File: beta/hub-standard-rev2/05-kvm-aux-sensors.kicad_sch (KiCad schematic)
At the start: 16 parts

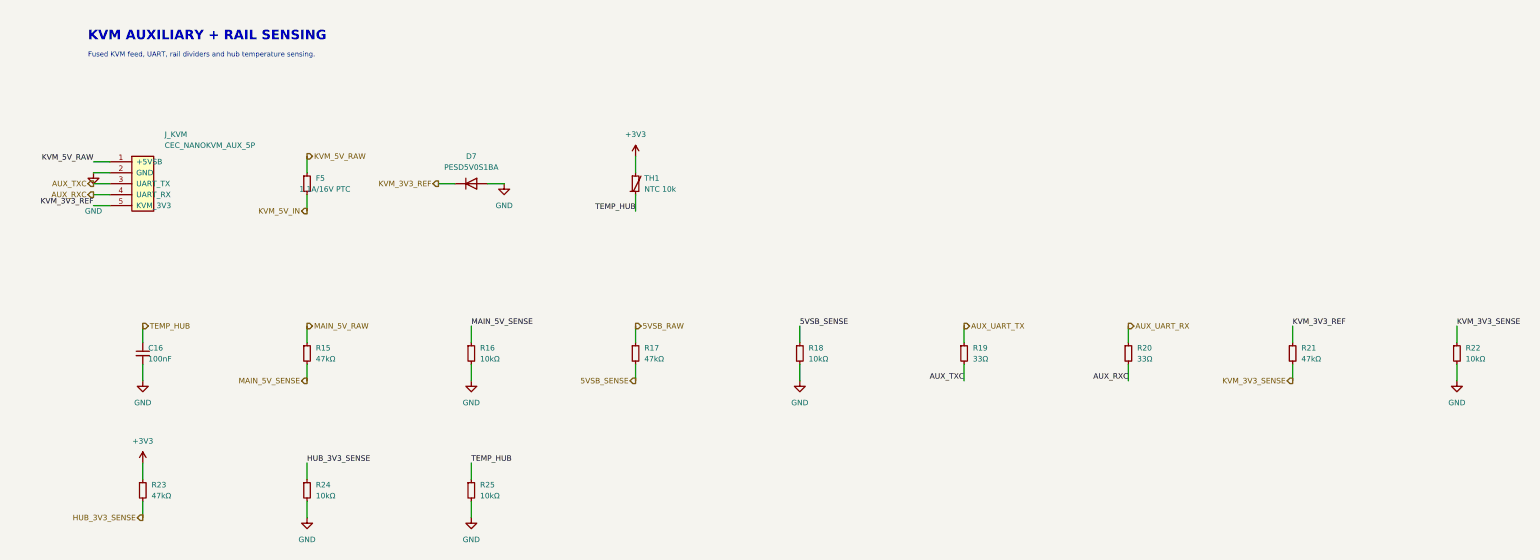
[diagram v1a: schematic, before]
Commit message: Rework BETA power rails and schematic composition
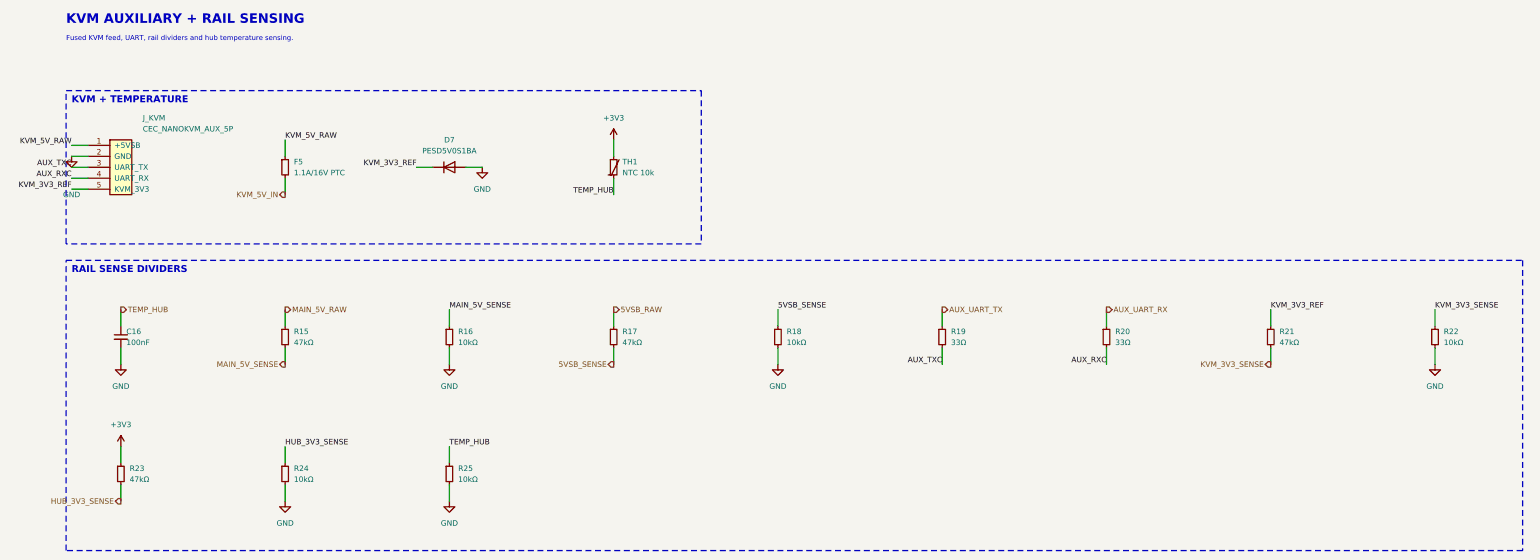
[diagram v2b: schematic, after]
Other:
- note added: "KVM + TEMPERATURE"
- note added: "RAIL SENSE DIVIDERS"

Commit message: pipeline: integrate route-aware physical design flow
Generalize critical-first placement and routing, future-congestion and power-authority planning, route provenance, process watchdogs, fab/thermal validation, dashboard review, and XFCN integration. Add the supporting board contracts, component libraries, documentation, and regression coverage.
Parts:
- removed R17: 47kΩ, cec-Resistor_SMD:R_0402_1005Metric, symbol cec-vendor:R_Small
- removed R18: 10kΩ, cec-Resistor_SMD:R_0402_1005Metric, symbol cec-vendor:R_Small
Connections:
- net MAIN_5V_RAW renamed +5V_SYS
- net MAIN_5V_SENSE renamed 5V_SYS_SENSE
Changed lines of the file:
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@@
-	)
-	(symbol
-		(lib_id "cec-vendor:R_Small")
-		(at 170.18 157.48 0)
-		(unit 1)
-		(exclude_from_sim no)
-		(in_bom yes)
-		(on_board yes)
-		(dnp no)
-		(fields_autoplaced yes)
-		(property "Reference" "R17" (at 172.212 156.21 0) (effects (font (size 1.27 1.27)) (justify left)))
-		(property "Value" "47kΩ" (at 172.212 158.75 0) (effects (font (size 1.27 1.27)) (justify left)))
-		(property "Footprint" "cec-Resistor_SMD:R_0402_1005Metric" (at 170.18 157.48 0) (effects (font (size 1.27 1.27)) (hide yes)))
-		(property "Datasheet" "" (at 170.18 157.48 0) (effects (font (size 1.27 1.27)) (hide yes)))
-		(property "Manufacturer" "UNI-ROYAL" (at 170.18 157.48 0) (effects (font (size 1.27 1.27)) (hide yes)))
-		(property "MPN" "0402WGF4702TCE" (at 170.18 157.48 0) (effects (font (size 1.27 1.27)) (hide yes)))
-		(property "LCSC" "C25792" (at 170.18 157.48 0) (effects (font (size 1.27 1.27)) (hide yes)))
-		(pin "1")
-		(pin "2")
-		(instances
-			(project "hub-standard-rev2"
-				(path "/aa22b2b4-0e2b-481a-a188-ee3f43fcbaa8/4c1dea1b-f0fd-55bf-9af5-1c20480c05cf" (reference "R17") (unit 1))
-			)
-		)
-	)
-	(symbol
-		(lib_id "cec-vendor:R_Small")
-		(at 208.28 157.48 0)
-		(unit 1)
-		(exclude_from_sim no)
-		(in_bom yes)
-		(on_board yes)
-		(dnp no)
-		(fields_autoplaced yes)
-		(property "Reference" "R18" (at 210.312 156.21 0) (effects (font (size 1.27 1.27)) (justify left)))
-		(property "Value" "10kΩ" (at 210.312 158.75 0) (effects (font (size 1.27 1.27)) (justify left)))
-		(property "Footprint" "cec-Resistor_SMD:R_0402_1005Metric" (at 208.28 157.48 0) (effects (font (size 1.27 1.27)) (hide yes)))
-		(property "Datasheet" "" (at 208.28 157.48 0) (effects (font (size 1.27 1.27)) (hide yes)))
-		(property "Manufacturer" "UNI-ROYAL" (at 208.28 157.48 0) (effects (font (size 1.27 1.27)) (hide yes)))
-		(property "MPN" "0402WGF1002TCE" (at 208.28 157.48 0) (effects (font (size 1.27 1.27)) (hide yes)))
-		(property "LCSC" "C25744" (at 208.28 157.48 0) (effects (font (size 1.27 1.27)) (hide yes)))
-		(pin "1")
-		(pin "2")
-		(instances
-			(project "hub-standard-rev2"
-				(path "/aa22b2b4-0e2b-481a-a188-ee3f43fcbaa8/4c1dea1b-f0fd-55bf-9af5-1c20480c05cf" (reference "R18") (unit 1))
-			)
-		)
 	)
 	(symbol
@@
 	(wire (pts (xy 170.18 115.57) (xy 170.18 111.76))
 		(stroke (width 0) (type default)))
-	(wire (pts (xy 170.18 154.94) (xy 170.18 151.13))
-		(stroke (width 0) (type default)))
-	(wire (pts (xy 170.18 160.02) (xy 170.18 163.83))
-		(stroke (width 0) (type default)))
-	(wire (pts (xy 208.28 154.94) (xy 208.28 151.13))
-		(stroke (width 0) (type default)))
 	(wire (pts (xy 284.48 154.94) (xy 284.48 151.13))
 		(stroke (width 0) (type default)))
@@
 	(wire (pts (xy 132.08 160.02) (xy 132.08 163.83))
 		(stroke (width 0) (type default)))
-	(wire (pts (xy 208.28 160.02) (xy 208.28 163.83))
-		(stroke (width 0) (type default)))
 	(wire (pts (xy 360.68 160.02) (xy 360.68 163.83))
 		(stroke (width 0) (type default)))
@@
 	(wire (pts (xy 132.08 191.77) (xy 132.08 195.58))
 		(stroke (width 0) (type default)))
-	(label "5VSB_SENSE" (at 208.28 151.13 0) (effects (font (size 1.27 1.27)) (justify left bottom)))
 	(label "HUB_3V3_SENSE" (at 93.98 182.88 0) (effects (font (size 1.27 1.27)) (justify left bottom)))
 	(label "AUX_RXC" (at 44.45 120.65 180) (effects (font (size 1.27 1.27)) (justify right bottom)))
@@
 	(label "KVM_5V_RAW" (at 44.45 113.03 180) (effects (font (size 1.27 1.27)) (justify right bottom)))
 	(label "KVM_3V3_SENSE" (at 360.68 151.13 0) (effects (font (size 1.27 1.27)) (justify left bottom)))
-	(label "MAIN_5V_SENSE" (at 132.08 151.13 0) (effects (font (size 1.27 1.27)) (justify left bottom)))
+	(label "5V_SYS_SENSE" (at 132.08 151.13 0) (effects (font (size 1.27 1.27)) (justify left bottom)))
 	(label "TEMP_HUB" (at 132.08 182.88 0) (effects (font (size 1.27 1.27)) (justify left bottom)))
 	(label "TEMP_HUB" (at 170.18 124.46 180) (effects (font (size 1.27 1.27)) (justify right bottom)))
-	(hierarchical_label "5VSB_RAW"
-		(shape output)
-		(at 170.18 151.13 0)
-		(effects (font (size 1.27 1.27)) (justify left))
-	)
-	(hierarchical_label "5VSB_SENSE"
-		(shape output)
-		(at 170.18 163.83 180)
-		(effects (font (size 1.27 1.27)) (justify right))
-	)
 	(hierarchical_label "AUX_UART_RX"
 		(shape output)
@@
 		(effects (font (size 1.27 1.27)) (justify right))
 	)
-	(hierarchical_label "MAIN_5V_RAW"
-		(shape output)
-		(at 93.98 151.13 0)
-		(effects (font (size 1.27 1.27)) (justify left))
-	)
-	(hierarchical_label "MAIN_5V_SENSE"
+	(hierarchical_label "5V_SYS_SENSE"
 		(shape output)
 		(at 93.98 163.83 180)
@@
 	(symbol
 		(lib_id "cec-power:GND")
-		(at 208.28 163.83 0)
-		(unit 1)
-		(exclude_from_sim no)
-		(in_bom yes)
-		(on_board yes)
-		(dnp no)
-		(property "Reference" "#PWR507" (at 208.28 161.29 0) (effects (font (size 1.27 1.27)) (hide yes)))
-		(property "Value" "GND" (at 208.28 168.91 0) (effects (font (size 1.27 1.27))))
-		(pin "1")
-		(instances
-			(project "hub-standard-rev2"
-				(path "/aa22b2b4-0e2b-481a-a188-ee3f43fcbaa8/4c1dea1b-f0fd-55bf-9af5-1c20480c05cf" (reference "#PWR507") (unit 1))
-			)
-		)
-	)
-	(symbol
-		(lib_id "cec-power:GND")
 		(at 360.68 163.83 0)
 		(unit 1)
@@
 		)
 	)
+	(global_label "+5V_SYS"
+		(shape passive)
+		(at 93.98 151.13 0)
+		(fields_autoplaced yes)
+		(effects (font (size 1.27 1.27)) (justify left bottom))
+		(property "Intersheetrefs" "${INTERSHEET_REFS}"
+			(at 93.98 151.13 0)
+			(effects (font (size 1.27 1.27)) (hide yes))
+		)
+	)
